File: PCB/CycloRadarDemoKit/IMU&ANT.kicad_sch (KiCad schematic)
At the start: 18 parts, among them J101 ANT_JTAG, U302 D52MxxM8, U502 MPU-6050

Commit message: PCB, 3Dmodel
mockup PCB version done, schcematic exported to latex, 3D model generated and exported to latex
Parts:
- J101: value ANT_JTAG -> ANT_SWD
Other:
- title: Safety Ride Radar Sensor -> Radar Safety Sensor
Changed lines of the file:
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@@
   (paper "A4")
   (title_block
-    (title "Safety Ride Radar Sensor")
-    (date "2023-12-19")
-    (rev "Rev.: WIP")
+    (title "Radar Safety Sensor")
+    (date "2023-12-20")
+    (rev "Rev.: 1")
     (company "ALPS Electric Czech, s.r.o.")
     (comment 1 "Designed by Martin Tavoda")
@@
     (stroke (width 0) (type default))
   )
-  (polyline (pts (xy 261.62 105.41) (xy 261.62 87.63))
+  (polyline (pts (xy 261.62 101.6) (xy 261.62 87.63))
     (stroke (width 0) (type dash))
   )
@@
       (effects (font (size 1.27 1.27)))
     )
-    (property "Value" "ANT_JTAG" (at 101.6 45.72 0)
-      (effects (font (size 1.27 1.27)))
-    )
+    (property "Value" "ANT_SWD" (at 101.6 45.72 0)
+      (effects (font (size 1.27 1.27)))
+    )

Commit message: PCB small updates, schemtatic cosmetics, SEP FINAL
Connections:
- net ~{SUSPEND}: now reaches TP502.1, U302.D4 (P022)
- net GPIO: now reaches TP503.1, U302.F1 (P025)
- net SLEEP: now reaches R503.1, TP501.1, U302.F5 (AIN4/P028)
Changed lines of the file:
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@@
+    (stroke (width 0) (type default))
+  )
+  (wire (pts (xy 173.99 76.2) (xy 189.23 76.2))
     (stroke (width 0) (type default))
   )
@@
   )
   (wire (pts (xy 135.89 81.28) (xy 143.51 81.28))
-    (stroke (width 0) (type default))
-  )
-  (wire (pts (xy 173.99 76.2) (xy 189.23 76.2))
     (stroke (width 0) (type default))
   )
@@
     (effects (font (size 1.27 1.27)) (justify left bottom))
   )
+  (label "~{SUSPEND}" (at 135.89 78.74 0) (fields_autoplaced)
+    (effects (font (size 0.762 0.762)) (justify left bottom))
+  )
   (label "BR2" (at 209.55 59.69 0) (fields_autoplaced)
     (effects (font (size 1.27 1.27)) (justify left bottom))
@@
     (effects (font (size 1.27 1.27)) (justify left bottom))
   )
+  (label "SLEEP" (at 179.07 76.2 0) (fields_autoplaced)
+    (effects (font (size 1.27 1.27)) (justify left bottom))
+  )
   (label "VCC" (at 93.98 49.53 180) (fields_autoplaced)
     (effects (font (size 1.27 1.27)) (justify right bottom))
@@
     (effects (font (size 1.27 1.27)) (justify left bottom))
   )
+  (label "GPIO" (at 135.89 83.82 0) (fields_autoplaced)
+    (effects (font (size 0.762 0.762)) (justify left bottom))
+  )
   (global_label "SDA" (shape bidirectional) (at 74.93 149.86 180) (fields_autoplaced)

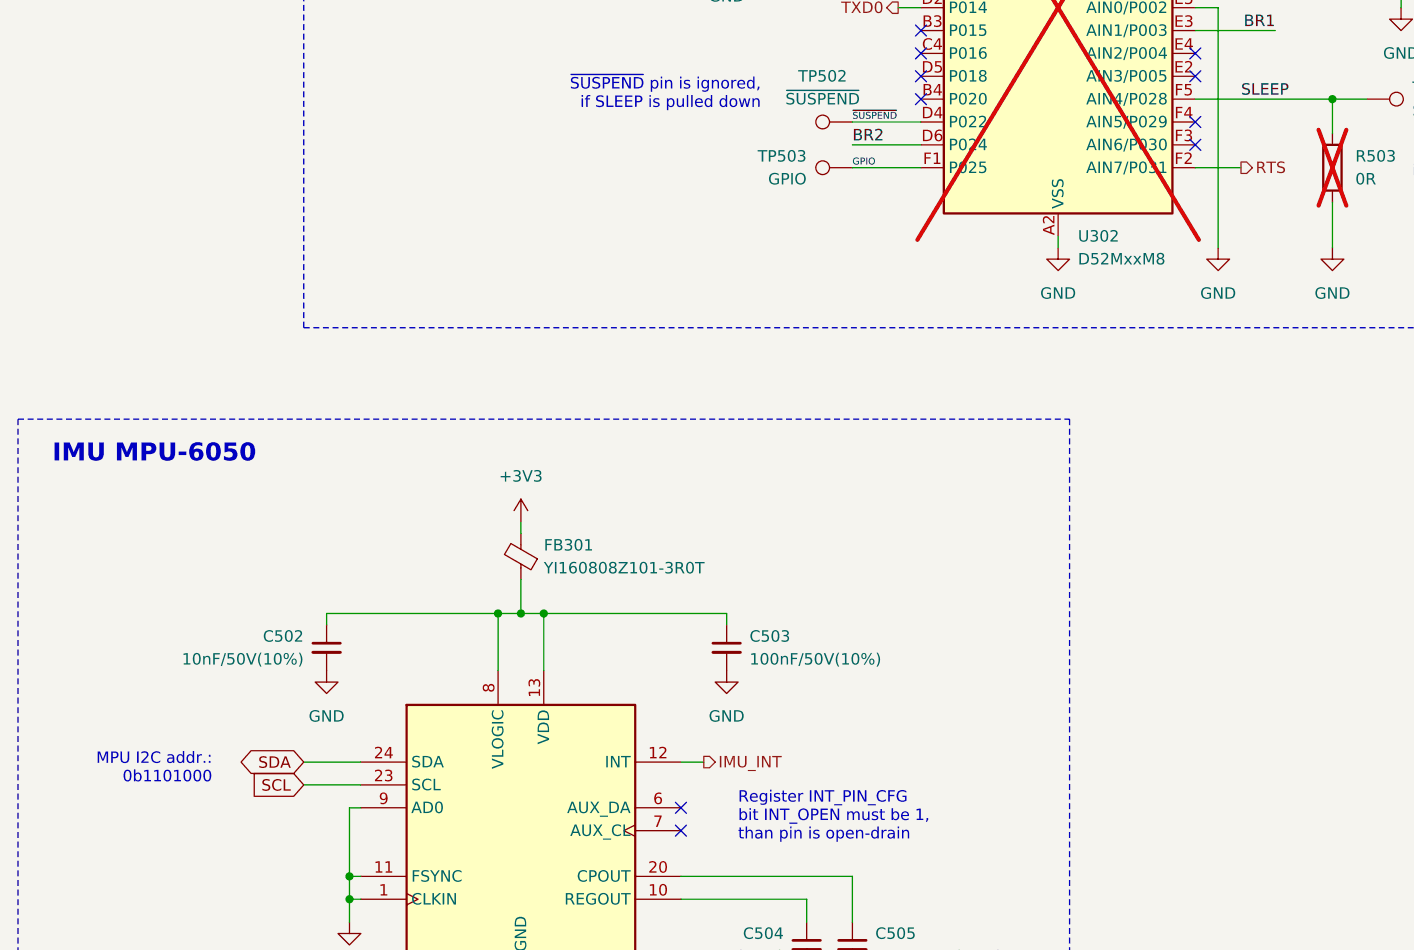
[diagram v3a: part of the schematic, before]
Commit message: All peripherals checked, changed ESP32 pinout
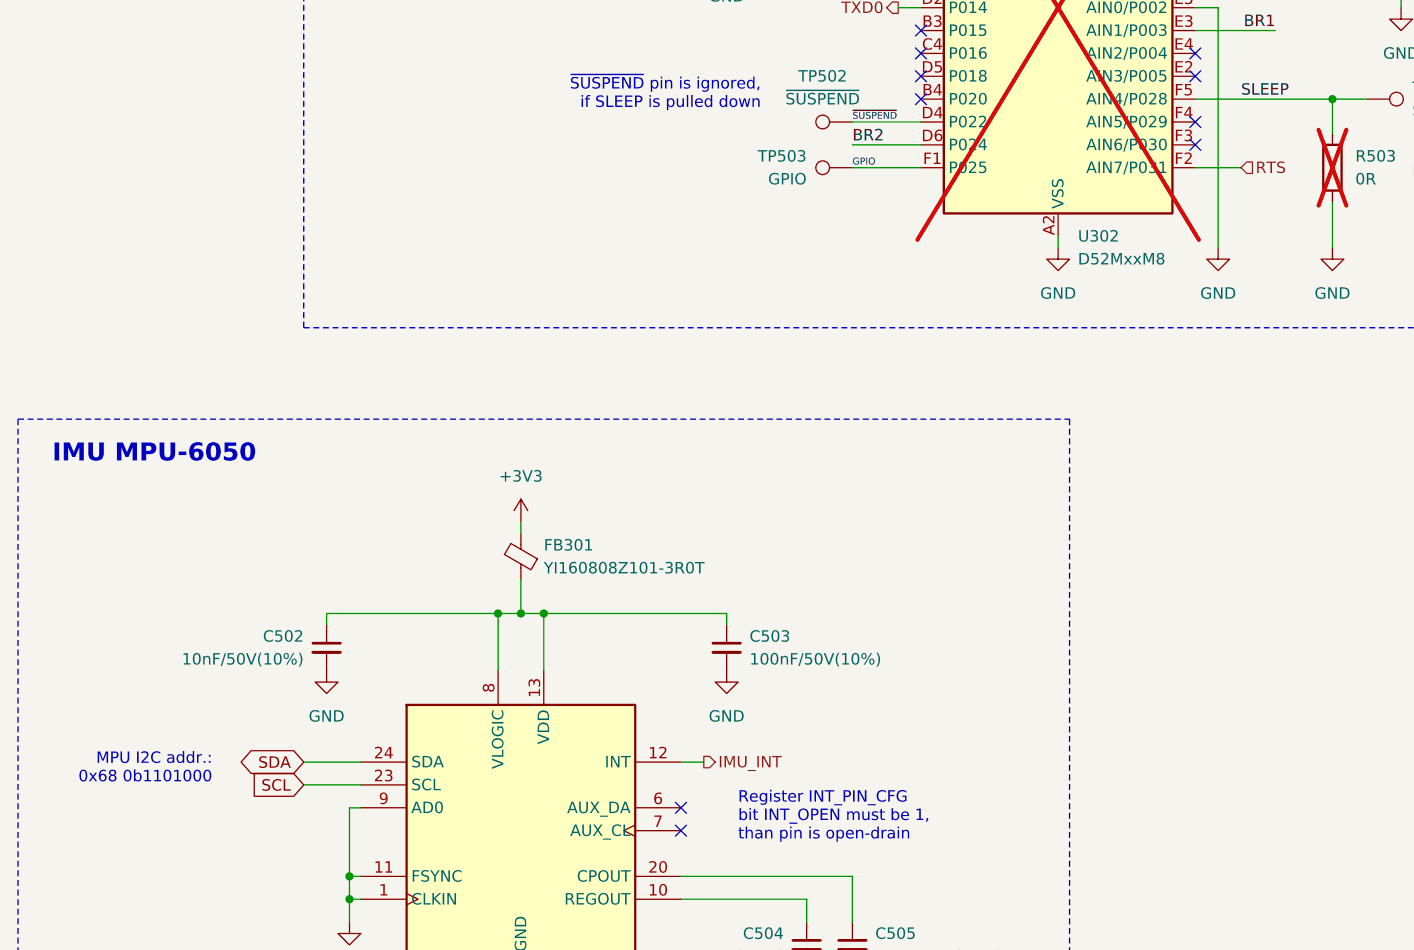
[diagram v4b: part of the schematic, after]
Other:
- note added: "MPU I2C addr.: 0x68 0b1101000"
- note removed: "MPU I2C addr.: 0b1101000"
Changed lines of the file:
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@@
     (effects (font (size 1.27 1.27)) (justify left bottom))
   )
-  (text "MPU I2C addr.: \n0b1101000\n" (at 64.77 152.4 0)
+  (text "MPU I2C addr.: \n0x68 0b1101000\n" (at 64.77 152.4 0)
     (effects (font (size 1.27 1.27)) (justify right bottom))
   )
@@
     )
   )
-  (hierarchical_label "RTS" (shape output) (at 179.07 83.82 0) (fields_autoplaced)
+  (hierarchical_label "RTS" (shape input) (at 179.07 83.82 0) (fields_autoplaced)
     (effects (font (size 1.27 1.27)) (justify left))
   )

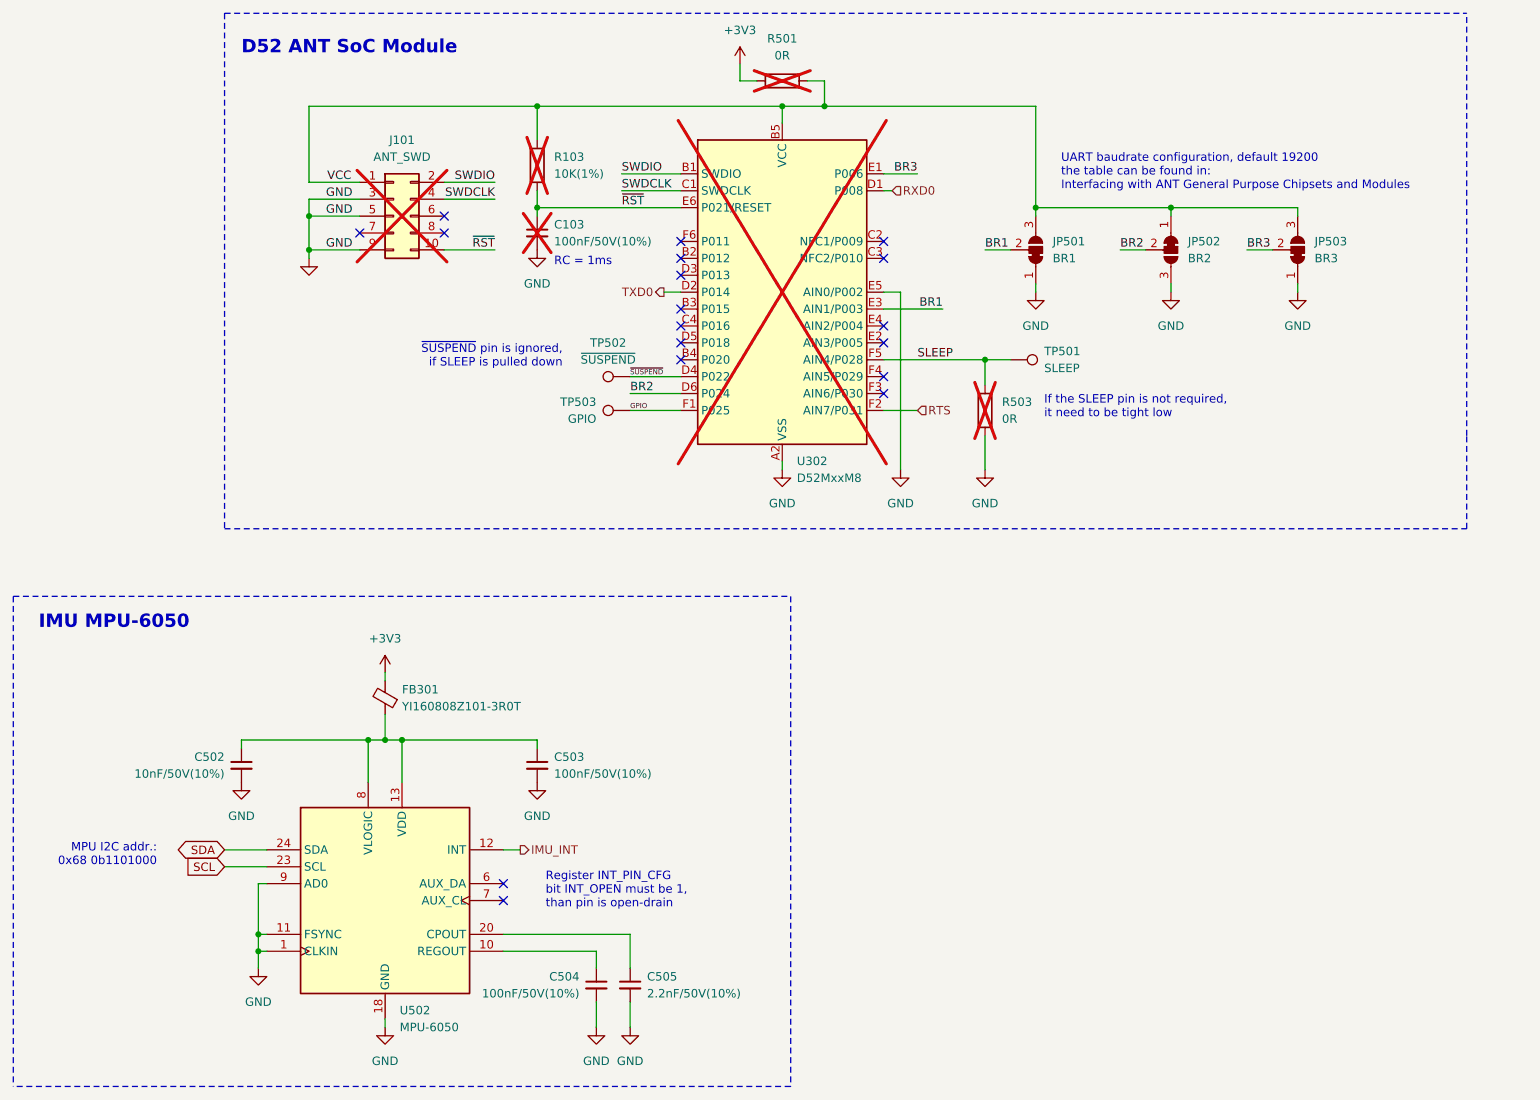
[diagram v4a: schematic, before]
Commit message: reanotated schematic, routing started
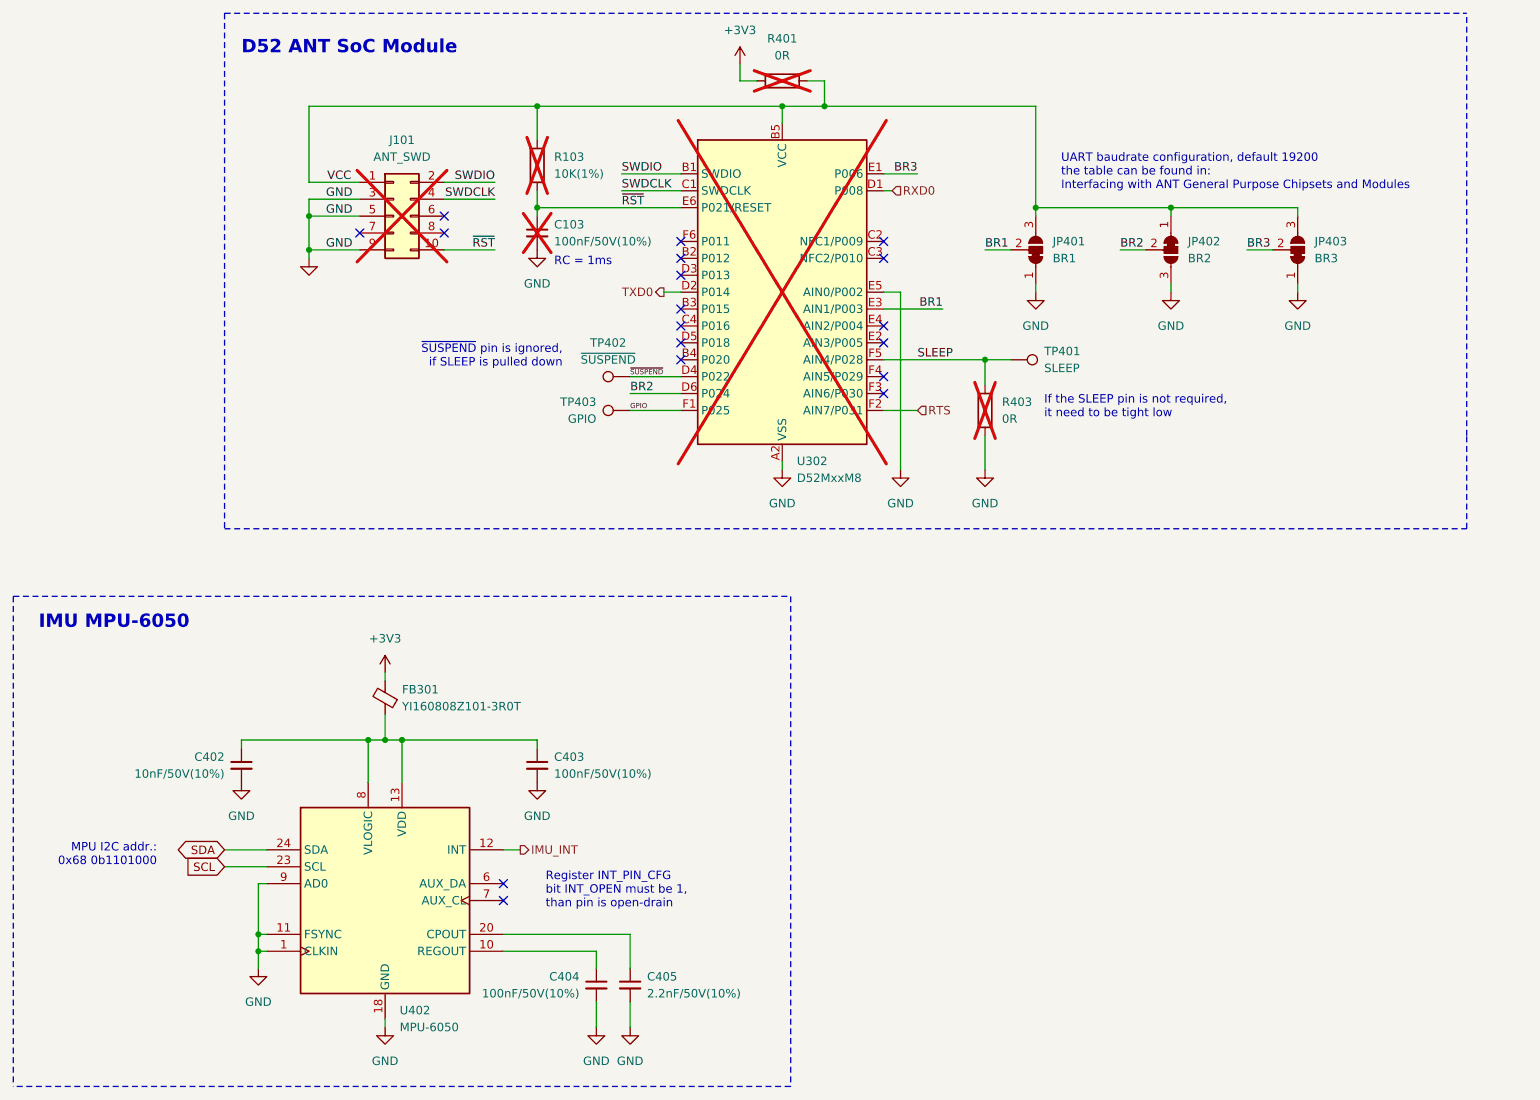
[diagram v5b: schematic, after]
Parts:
- renumbered C502 to C402, C503 to C403, C504 to C404, C505 to C405, JP501 to JP401, JP502 to JP402, JP503 to JP403, R501 to R401, R503 to R403, TP501 to TP401, TP502 to TP402, TP503 to TP403, U502 to U402

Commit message: USB layout, long traces from upper prepaired
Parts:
- JP401, JP402, JP403, TP401, TP402, TP403: now left out of the parts list
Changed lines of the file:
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@@
   )
   (symbol (lib_id "Jumper:SolderJumper_3_Bridged12") (at 236.22 59.69 270) (mirror x) (unit 1)
-    (in_bom yes) (on_board yes) (dnp no) (fields_autoplaced)
+    (in_bom no) (on_board yes) (dnp no) (fields_autoplaced)
     (property "Reference" "JP403" (at 238.76 58.42 90)
       (effects (font (size 1.27 1.27)) (justify left))
@@
   )
   (symbol (lib_id "Connector:TestPoint") (at 135.89 83.82 90) (unit 1)
-    (in_bom yes) (on_board yes) (dnp no) (fields_autoplaced)
+    (in_bom no) (on_board yes) (dnp no) (fields_autoplaced)
     (property "Reference" "TP403" (at 130.81 82.55 90)
       (effects (font (size 1.27 1.27)) (justify left))
@@
   )
   (symbol (lib_id "Jumper:SolderJumper_3_Bridged12") (at 196.85 59.69 270) (mirror x) (unit 1)
-    (in_bom yes) (on_board yes) (dnp no) (fields_autoplaced)
+    (in_bom no) (on_board yes) (dnp no) (fields_autoplaced)
     (property "Reference" "JP401" (at 199.39 58.42 90)
       (effects (font (size 1.27 1.27)) (justify left))
@@
   )
   (symbol (lib_id "Connector:TestPoint") (at 193.04 76.2 270) (unit 1)
-    (in_bom yes) (on_board yes) (dnp no) (fields_autoplaced)
+    (in_bom no) (on_board yes) (dnp no) (fields_autoplaced)
     (property "Reference" "TP401" (at 198.12 74.93 90)
       (effects (font (size 1.27 1.27)) (justify left))
@@
   )
   (symbol (lib_id "Jumper:SolderJumper_3_Bridged12") (at 217.17 59.69 270) (unit 1)
-    (in_bom yes) (on_board yes) (dnp no) (fields_autoplaced)
+    (in_bom no) (on_board yes) (dnp no) (fields_autoplaced)
     (property "Reference" "JP402" (at 219.71 58.42 90)
       (effects (font (size 1.27 1.27)) (justify left))
@@
   )
   (symbol (lib_id "Connector:TestPoint") (at 135.89 78.74 90) (unit 1)
-    (in_bom yes) (on_board yes) (dnp no) (fields_autoplaced)
+    (in_bom no) (on_board yes) (dnp no) (fields_autoplaced)
     (property "Reference" "TP402" (at 132.588 73.66 90)
       (effects (font (size 1.27 1.27)))

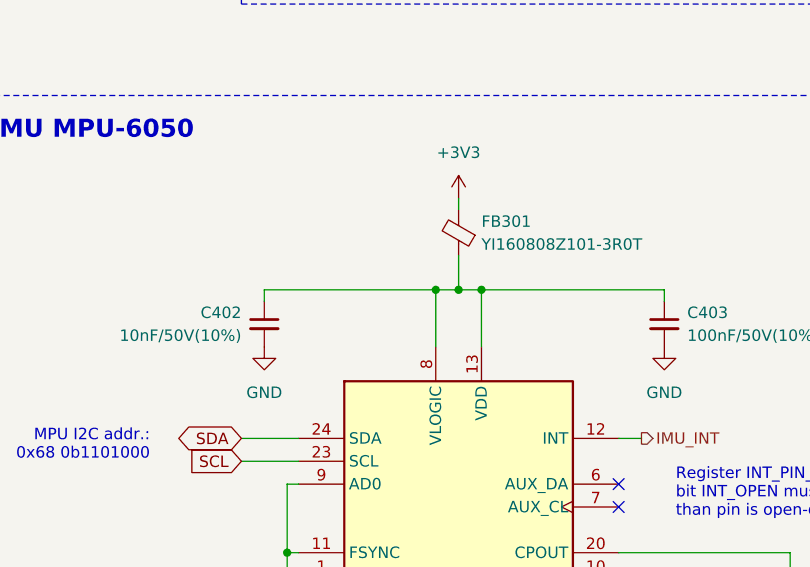
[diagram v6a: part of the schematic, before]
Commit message: DC/DC routed, stuckup properties changed
ready for PCB resize
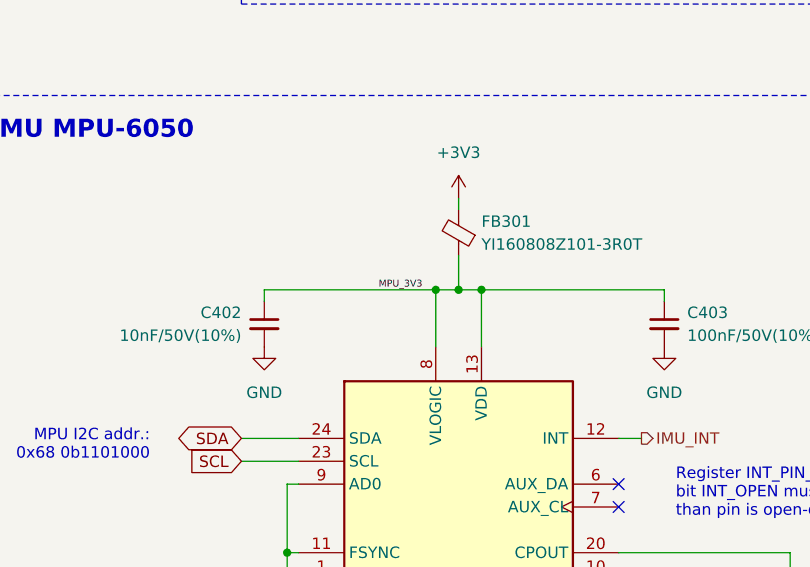
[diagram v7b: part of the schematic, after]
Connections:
- net MPU_3V3: now reaches C402.1, C403.1, FB301.1, U402.13 (VDD), U402.8 (VLOGIC)

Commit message: start of repair after review
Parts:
- C103, J101, R103, R401, R403, U302: now left out of the parts list
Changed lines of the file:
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@@
   )
   (symbol (lib_id "Device:C_Small") (at 121.92 57.15 0) (unit 1)
-    (in_bom yes) (on_board yes) (dnp yes) (fields_autoplaced)
+    (in_bom no) (on_board yes) (dnp yes) (fields_autoplaced)
     (property "Reference" "C103" (at 124.46 55.8863 0)
       (effects (font (size 1.27 1.27)) (justify left))
@@
   )
   (symbol (lib_id "RF_Module:D52MxxM8") (at 158.75 66.04 0) (unit 1)
-    (in_bom yes) (on_board yes) (dnp yes) (fields_autoplaced)
+    (in_bom no) (on_board yes) (dnp yes) (fields_autoplaced)
     (property "Reference" "U302" (at 160.9441 91.44 0)
       (effects (font (size 1.27 1.27)) (justify left))
@@
   )
   (symbol (lib_id "Device:R") (at 158.75 34.29 90) (unit 1)
-    (in_bom yes) (on_board yes) (dnp yes) (fields_autoplaced)
+    (in_bom no) (on_board yes) (dnp yes) (fields_autoplaced)
     (property "Reference" "R401" (at 158.75 27.94 90)
       (effects (font (size 1.27 1.27)))
@@
   )
   (symbol (lib_id "Device:R") (at 189.23 83.82 0) (unit 1)
-    (in_bom yes) (on_board yes) (dnp yes) (fields_autoplaced)
+    (in_bom no) (on_board yes) (dnp yes) (fields_autoplaced)
     (property "Reference" "R403" (at 191.77 82.55 0)
       (effects (font (size 1.27 1.27)) (justify left))
@@
   )
   (symbol (lib_id "Device:R") (at 121.92 46.99 0) (mirror x) (unit 1)
-    (in_bom yes) (on_board yes) (dnp yes) (fields_autoplaced)
+    (in_bom no) (on_board yes) (dnp yes) (fields_autoplaced)
     (property "Reference" "R103" (at 124.46 45.72 0)
       (effects (font (size 1.27 1.27)) (justify left))
@@
   )
   (symbol (lib_id "Connector_Generic:Conn_02x05_Odd_Even") (at 100.33 54.61 0) (unit 1)
-    (in_bom yes) (on_board yes) (dnp yes) (fields_autoplaced)
+    (in_bom no) (on_board yes) (dnp yes) (fields_autoplaced)
     (property "Reference" "J101" (at 101.6 43.18 0)
       (effects (font (size 1.27 1.27)))
